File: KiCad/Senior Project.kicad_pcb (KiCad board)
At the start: 4 copper layers, 59.2 x 89.2 mm, 69 parts, among them J1 USB_C_Receptacle_USB2.0_16P, J2 Screw_Terminal_01x02, J3 Screw_Terminal_01x06, Q2 IRLML0030, Q3 IRLML0030, Q4 IRLML0030, SW1 SW_Push, SW2 SW_Push, U1 ESP32-S3FH4R2, U2 TPS62162DSG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

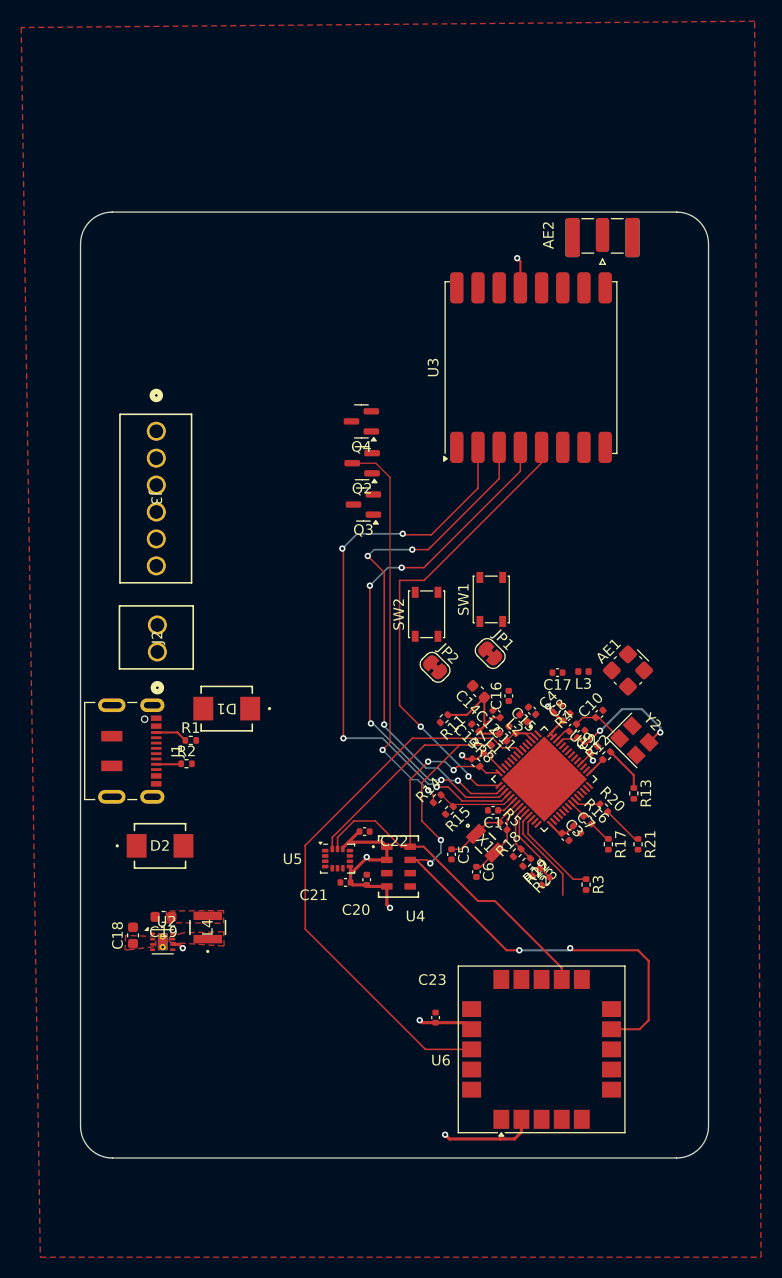
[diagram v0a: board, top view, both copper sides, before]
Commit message: Added power routing moved usb, and routed a couple signals to radio
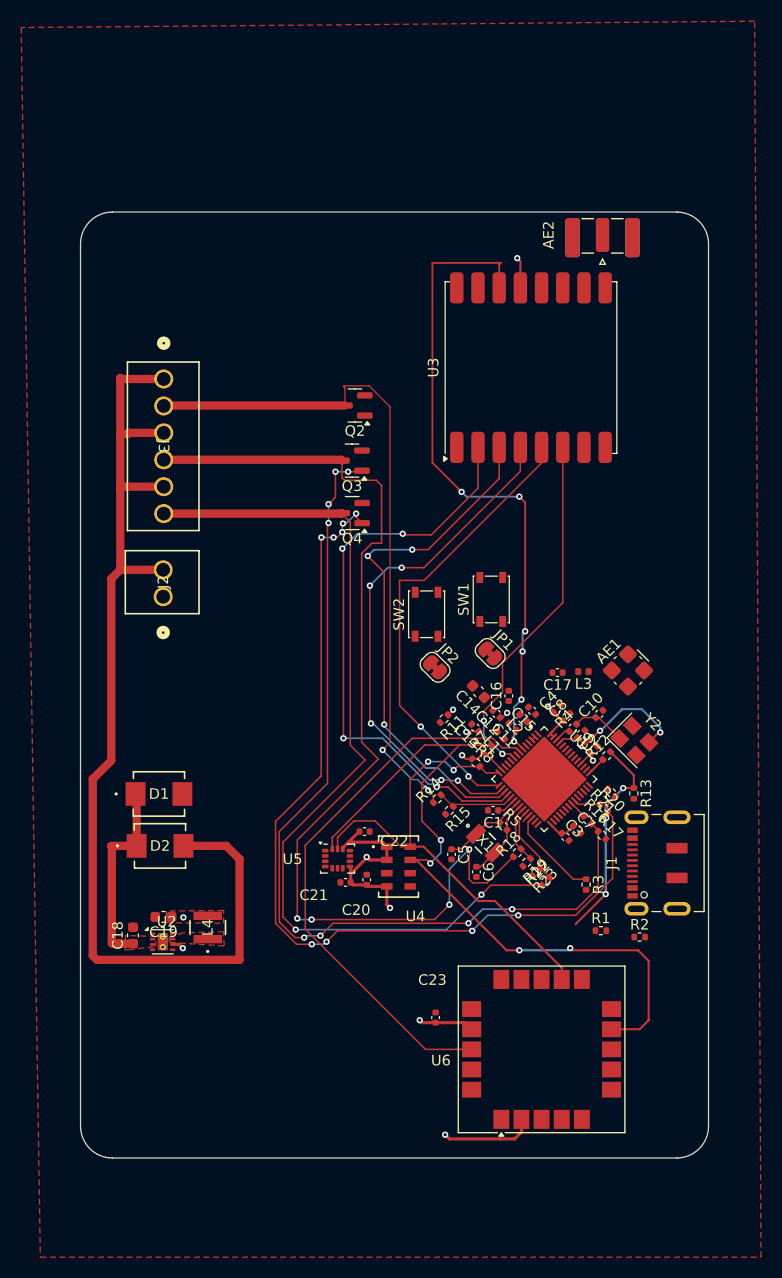
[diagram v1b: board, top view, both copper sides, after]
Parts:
- moved J1 52.1 mm to (179.1, 111.2), turned to 90 degrees
- moved R2 45.8 mm to (176.8, 118.2)
- moved R1 42.7 mm to (173.1, 117.5)
- moved D1 10.3 mm to (131.4, 104.7), turned to 0 degrees
- moved Q4 8.69 mm to (149.6, 78.2)
- moved Q2 5.49 mm to (149.9, 68.0)
- moved R21 5.46 mm to (174.1, 104.5), turned to 135 degrees
- moved J2 5.24 mm to (131.8, 86.0)
- moved J3 4.98 mm to (131.8, 65.5)
- moved Q3 4.28 mm to (149.6, 73.2)
- moved R17 1.04 mm to (173.2, 108.5), turned to -45 degrees
- moved C11 0.29 mm to (164.8, 98.3)
- moved L1 0.26 mm to (163.6, 99.1)
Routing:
- net +BATT: track 0.00 -> 101.4 mm
- net /Pyro Channel2/Pyro Pin: track 0.00 -> 97.6 mm, vias 0 -> 4
- net /Pyro Channel3/Pyro Pin: track 0.00 -> 85.7 mm, vias 0 -> 2
- net Net-(Q3-G): track 2.18 -> 86.1 mm, vias 0 -> 8
- net Net-(Q4-G): track 3.94 -> 87.5 mm, vias 0 -> 9
- net /Interrupt: track 0.00 -> 62.1 mm, vias 0 -> 6
- net /RADIO_RST: track 0.00 -> 34.0 mm, vias 0 -> 2
- net /Pyro Channel1/Pyro Pin: track 37.4 -> 64.1 mm
- net +VDC: track 0.00 -> 18.6 mm
- net Net-(Q2-G): track 4.32 -> 20.0 mm, vias 0 -> 2
- net +3V3: track 59.4 -> 50.2 mm, vias 9 -> 13
- net /USB_D-: track 9.32 -> 0.79 mm
- net /ESP-32 Power Coupler/VDD3P3: track 4.87 -> 0.59 mm
- net Net-(J1-CC1): track 3.05 -> 0.00 mm
- net Net-(J1-CC2): track 2.36 -> 0.00 mm
- added copper zone on In2.Cu, net +3V3
- removed copper zone on In1.Cu, net +3V3

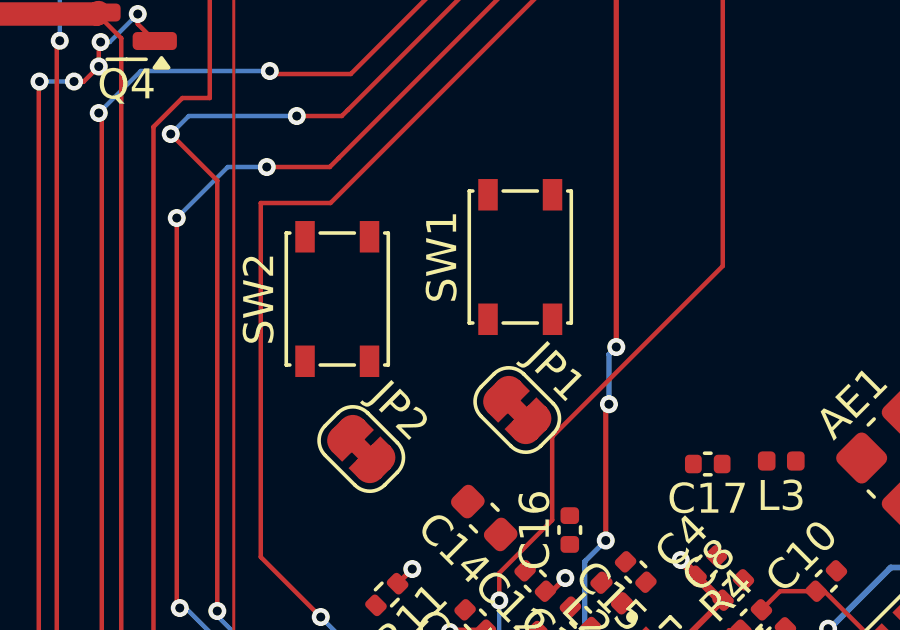
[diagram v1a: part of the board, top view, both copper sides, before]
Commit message: Added power routing moved usb, and more routing
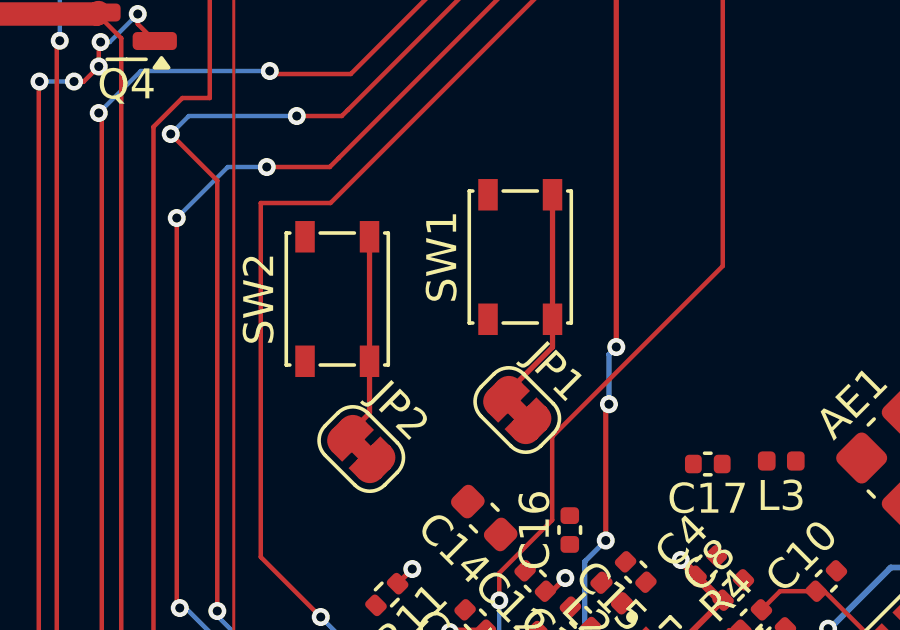
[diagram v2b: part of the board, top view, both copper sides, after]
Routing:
- net Net-(JP1-A): track 0.00 -> 7.39 mm
- net Net-(JP2-A): track 0.00 -> 6.92 mm
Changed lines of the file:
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@@
+	)
+	(segment
+		(start 163.825 88.375)
+		(end 163.825 84.225)
+		(width 0.175)
+		(layer "F.Cu")
+		(net 20)
+	)
+	(segment
+		(start 162.190381 90.940381)
+		(end 163.825 89.305762)
+		(width 0.175)
+		(layer "F.Cu")
+		(net 20)
+	)
+	(segment
+		(start 163.825 89.305762)
+		(end 163.825 88.375)
+		(width 0.175)
+		(layer "F.Cu")
+		(net 20)
+	)
+	(segment
+		(start 157.725 89.775)
+		(end 157.725 85.625)
+		(width 0.175)
+		(layer "F.Cu")
+		(net 23)
+	)
+	(segment
+		(start 157.725 91.505762)
+		(end 157.725 89.775)
+		(width 0.175)
+		(layer "F.Cu")
+		(net 23)
+	)
+	(segment
+		(start 156.990381 92.240381)
+		(end 157.725 91.505762)
+		(width 0.175)
+		(layer "F.Cu")
+		(net 23)
 	)
 	(segment

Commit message: Routing and placement
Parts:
- removed AE1: Antenna_Shield, RF_Antenna:Molex_47948-0001_2.4Ghz
- removed C10: 15p, Capacitor_SMD:C_0402_1005Metric
- removed C11, C12, C15, C16, C17, C9: 0.1uF, Capacitor_SMD:C_0402_1005Metric
- removed C13, C7, C8: 1uF, Capacitor_SMD:C_0402_1005Metric
- removed C14: 10uF, Capacitor_SMD:C_0603_1608Metric
- removed C5: 20pf, Capacitor_SMD:C_0402_1005Metric
- removed C6: 20p, Capacitor_SMD:C_0402_1005Metric
- removed JP1, JP2: SolderJumper_2_Bridged, Jumper:SolderJumper-2_P1.3mm_Bridged_RoundedPad1.0x1.5mm
- removed L1, L2, L3: 2.0nH, Inductor_SMD:L_0402_1005Metric
- removed R11: 100k, Resistor_SMD:R_0402_1005Metric
- removed R5: TBD, Capacitor_SMD:C_0402_1005Metric
- removed R7, R8: 10k, Resistor_SMD:R_0402_1005Metric
- removed SW2: SW_Push, Button_Switch_SMD:SW_SPST_PTS810
- removed X1: FC-135 32.7680KA-A5, FC-135:XTAL_FC-135_EPS
- removed Y2: Crystal_GND23, Crystal:Crystal_SMD_3225-4Pin_3.2x2.5mm
- added J5: Conn_01x03, Connector_PinHeader_2.54mm:PinHeader_1x03_P2.54mm_Vertical, F.Cu at (139.2, 87.3)
- C1: value 0.1uF -> 22 uF
- C2: value 15p -> 0.1 uF
- C3: value 0.1uF -> 0.1 uF
- C4: value 10nF -> 1 uF
- R4: value 24 nF -> 10k; footprint Capacitor_SMD:C_0402_1005Metric -> Resistor_SMD:R_0402_1005Metric
- U1: value ESP32-S3FH4R2 -> ESP32-S3-WROOM-1; footprint S3FH4R2:QFN40P700X700X90-57N -> RF_Module:ESP32-S3-WROOM-1U
- moved R20 38.7 mm to (151.1, 74.3)
- moved R12 38.7 mm to (151.3, 69.4)
- moved R13 38.7 mm to (153.9, 72.9)
- moved R16 38.7 mm to (149.6, 75.4)
- moved R17 38.7 mm to (150.9, 76.9)
- moved R21 38.7 mm to (151.8, 72.9)
- moved R19 30.3 mm to (142.0, 92.7), turned to 135 degrees
- moved R18 28.9 mm to (142.9, 91.8), turned to -45 degrees
- moved SW1 27.5 mm to (150.8, 111.1), turned to 180 degrees
- moved R2 23.0 mm to (173.6, 95.4), turned to 90 degrees
- moved R15 21.9 mm to (140.9, 93.6), turned to 135 degrees
- moved R14 20.8 mm to (139.8, 94.5), turned to -45 degrees
- moved C2 17.8 mm to (157.2, 109.9)
- moved R1 17.5 mm to (173.8, 100.1), turned to -90 degrees
- moved C4 16.2 mm to (160.9, 110.7)
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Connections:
- C2 pad 1: GND -> +3V3
- C2 pad 2: Net-(U1-XTAL_N) -> GND
- C3 pad 1: Net-(U1-VDD_SPI) -> GND
- C3 pad 2: GND -> /EN
- C4 pad 1: +3V3 -> GND
- C4 pad 2: GND -> /EN
- R4 pad 1: Net-(U1-XTAL_P) -> +3V3
- R4 pad 2: Net-(C10-Pad1) -> /EN
- SW1 pad 2: Net-(JP1-A) -> /EN
- U1 pad 1: /LNA Shield/LNA_IN -> GND
- U1 pad 10: unconnected-(U1-GPIO5-Pad10) -> /Pyro GPIO 1
- U1 pad 11: unconnected-(U1-GPIO6-Pad11) -> /Pyro GPIO 2
- U1 pad 13: /SDA -> /USB_D-
- U1 pad 14: /SCL -> /USB_D+
- U1 pad 15: /FSPICS0 -> unconnected-(U1-GPIO3/TOUCH3/ADC1_CH2-Pad15)
- U1 pad 16: /FSPID -> unconnected-(U1-GPIO46-Pad16)
- U1 pad 17: /FSPICLK -> /Interrupt
- U1 pad 18: /FSPIQ -> /FSPICS0
- U1 pad 19: /Sense 1 -> /FSPID
- U1 pad 2: /ESP-32 Power Coupler/VDD3P3 -> +3V3
- U1 pad 20: +3V3 -> /FSPICLK
- U1 pad 21: Net-(U1-XTAL_32K_P) -> /FSPIQ
- U1 pad 22: Net-(U1-XTAL_32K_N) -> /RADIO_RST
- U1 pad 23: /Sense 2 -> /Pyro GPIO 3
- U1 pad 24: /Sense 3 -> unconnected-(U1-GPIO47/SPICLK_P/SUBSPICLK_P_DIFF-Pad24)
- U1 pad 25: /USB_D- -> unconnected-(U1-GPIO48/SPICLK_N/SUBSPICLK_N_DIFF-Pad25)
- U1 pad 26: /USB_D+ -> unconnected-(U1-GPIO45-Pad26)
- U1 pad 29: Net-(U1-VDD_SPI) -> unconnected-(U1-SPIIO7/GPIO36/FSPICLK/SUBSPICLK-Pad29)
- U1 pad 3: /ESP-32 Power Coupler/VDD3P3 -> /EN
- U1 pad 32: unconnected-(U1-GPIO29/SPICS0-Pad32) -> /MTCK
- U1 pad 33: unconnected-(U1-GPIO30/SPICLK-Pad33) -> /MTD0
- U1 pad 34: unconnected-(U1-GPIO31/SPIQ-Pad34) -> /MTDI
- U1 pad 35: unconnected-(U1-GPIO32/SPID-Pad35) -> /MTMS
- U1 pad 36: /Pyro GPIO 2 -> /UORXD
- U1 pad 37: /Pyro GPIO 3 -> /UOTXD
- U1 pad 38: unconnected-(U1-GPIO33-Pad38) -> /Sense 2
- U1 pad 39: unconnected-(U1-GPIO34-Pad39) -> /Sense 1
- U1 pad 4: Net-(JP1-B) -> /GPS_Reset
- U1 pad 40: unconnected-(U1-GPIO35-Pad40) -> GND
- U1 pad 41: unconnected-(U1-GPIO36-Pad41) -> GND
- U1 pad 5: Net-(JP2-B) -> /SCL
- U1 pad 6: /Interrupt -> /SDA
- U1 pad 7: /GPS_Reset -> /Sense 3
- U1 pad 9: /RADIO_RST -> unconnected-(U1-GPIO16/U0CTS/ADC2_CH5/XTAL_32K_N-Pad9)
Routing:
- net +BATT: track 101.4 -> 0.00 mm
- net /Pyro Channel2/Pyro Pin: track 97.6 -> 0.00 mm, vias 4 -> 0
- net Net-(Q4-G): track 87.5 -> 0.00 mm, vias 9 -> 0
- net Net-(Q3-G): track 86.1 -> 0.00 mm, vias 8 -> 0
- net /Pyro Channel3/Pyro Pin: track 85.7 -> 0.00 mm, vias 2 -> 0
- net /Pyro Channel1/Pyro Pin: track 64.1 -> 0.00 mm, vias 2 -> 0
- net /Interrupt: track 62.1 -> 0.00 mm, vias 6 -> 0
- net /FSPIQ: track 55.3 -> 0.00 mm, vias 4 -> 0
- net /FSPICLK: track 49.7 -> 0.00 mm, vias 4 -> 0
- net /FSPID: track 49.0 -> 0.00 mm, vias 4 -> 0
- net /FSPICS0: track 43.9 -> 0.00 mm, vias 2 -> 0
- net GND: track 1.26 -> 37.2 mm
- net /RADIO_RST: track 34.0 -> 0.00 mm, vias 2 -> 0
- net /SDA: track 74.4 -> 45.1 mm, vias 4 -> 0
- net /GPS_Reset: track 53.3 -> 28.9 mm
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
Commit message: Routing
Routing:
- net /SDA: track 45.1 -> 85.0 mm, vias 0 -> 2
- net /SCL: track 35.7 -> 61.4 mm, vias 0 -> 2
- net /RADIO_RST: track 0.00 -> 22.0 mm, vias 0 -> 4
- net /FSPICS0: track 0.00 -> 20.7 mm
- net /FSPICLK: track 0.00 -> 19.0 mm, vias 0 -> 2
- net /FSPID: track 0.00 -> 18.5 mm
- net /FSPIQ: track 0.00 -> 16.7 mm
- net /Pyro GPIO 3: track 0.00 -> 3.94 mm
- net /GPS_Reset: track 28.9 -> 29.7 mm, vias 0 -> 2

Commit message: More routing
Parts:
- moved R13 7.01 mm to (148.9, 68.0), turned to 0 degrees
- moved R21 5.78 mm to (148.8, 77.8), turned to 0 degrees
- moved R20 5.23 mm to (148.8, 79.0), turned to 180 degrees
- moved R17 4.39 mm to (148.8, 73.0), turned to 0 degrees
- moved R12 2.45 mm to (148.9, 69.1), turned to 180 degrees
- moved R16 1.51 mm to (148.8, 74.1), turned to 180 degrees
- moved J1 0.81 mm to (179.2, 97.6)
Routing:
- net /Pyro Channel1/Pyro Pin: track 0.00 -> 12.6 mm
- net /Pyro Channel2/Pyro Pin: track 0.00 -> 12.4 mm
- net /Pyro Channel3/Pyro Pin: track 0.00 -> 12.4 mm
- net /Sense 1: track 0.00 -> 4.24 mm
- net /SDA: track 85.0 -> 81.1 mm
- net /Sense 2: track 0.00 -> 3.28 mm

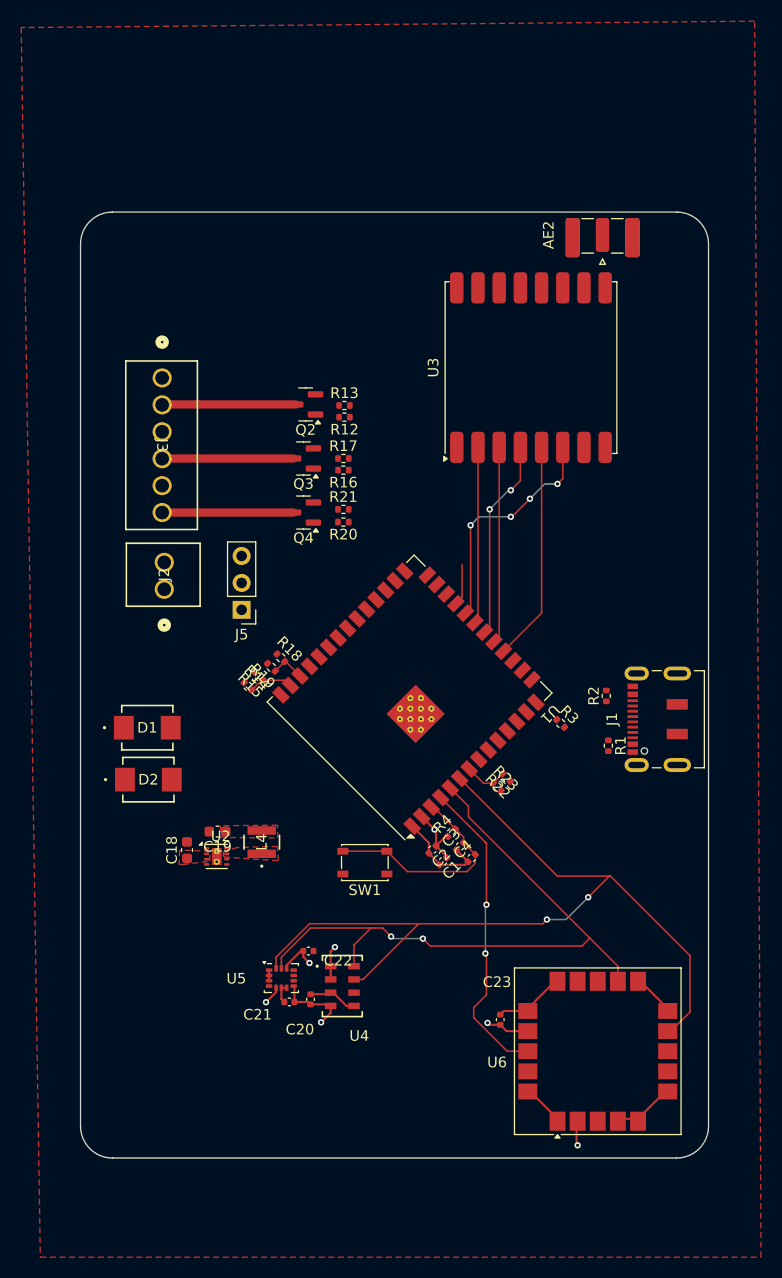
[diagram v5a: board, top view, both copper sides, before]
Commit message: DRC issues, only a few signals left to be routed
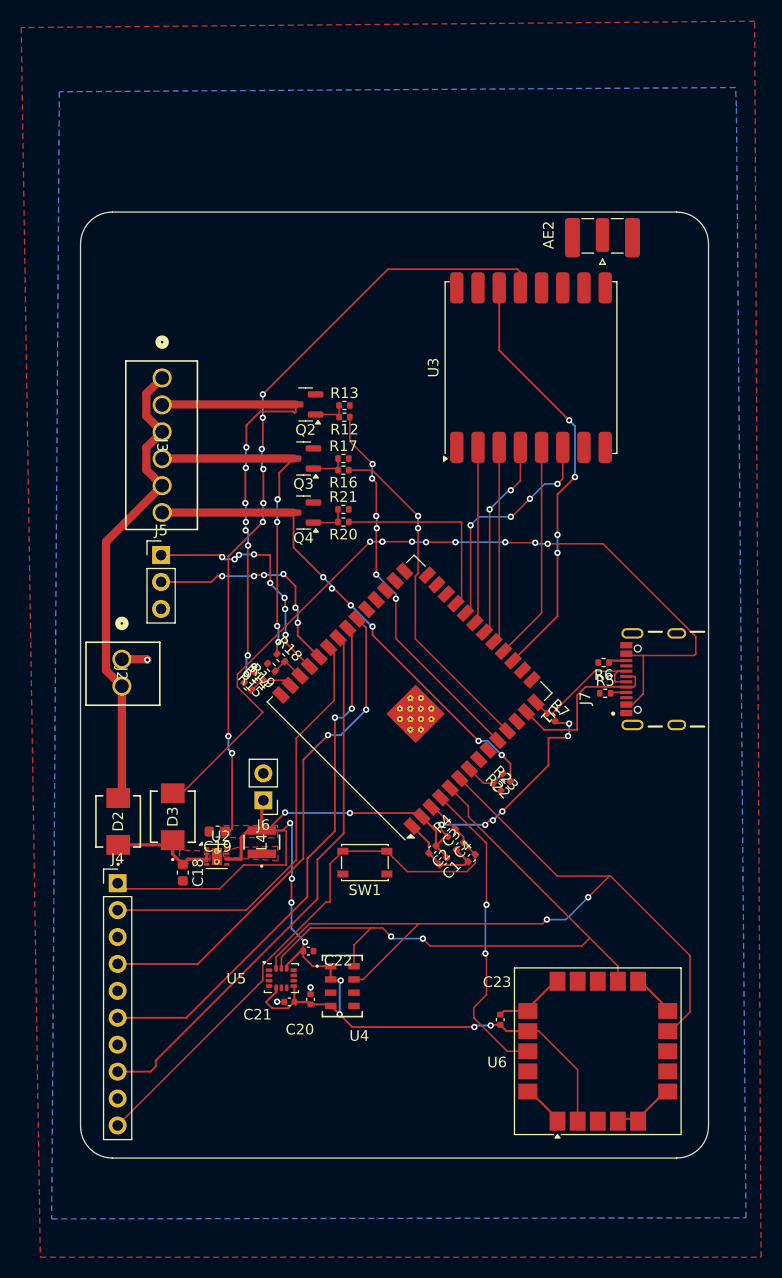
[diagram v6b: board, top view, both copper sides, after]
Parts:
- removed D1: D, VS_10BQ015HM3_5BT:CR_SMBDO-214AA_VIS
- removed J1: USB_C_Receptacle_USB2.0_16P, Connector_USB:USB_C_Receptacle_JAE_DX07S016JA1R1500
- removed R1, R2: 5.1k, Resistor_SMD:R_0402_1005Metric
- removed R3: 100k, Resistor_SMD:R_0402_1005Metric
- added D3: D, VS_10BQ015HM3_5BT:CR_SMBDO-214AA_VIS, F.Cu at (132.7, 106.8)
- added J4: Conn_ARM_JTAG_SWD_10, Connector_PinHeader_2.54mm:PinHeader_1x10_P2.54mm_Vertical, F.Cu at (127.5, 113.1)
- added J6: Conn_01x02, Connector_PinHeader_2.54mm:PinHeader_1x02_P2.54mm_Vertical, F.Cu at (141.2, 105.2)
- added J7: USB4105-GF-A, USB4105_GF_A (1):GCT_USB4105-GF-A, F.Cu at (180.2, 93.8)
- added R5: 5.1k, Resistor_SMD:R_0402_1005Metric, F.Cu at (173.5, 95.2)
- added R6: 5.1k, Resistor_SMD:R_0402_1005Metric, F.Cu at (173.3, 92.2)
- added R7: 100k, Resistor_SMD:R_0402_1005Metric, F.Cu at (168.4, 97.4)
- moved J5 9.19 mm to (131.6, 82.1), turned to 0 degrees
- moved J2 7.72 mm to (127.9, 91.9), turned to -90 degrees
- moved D2 4.87 mm to (127.5, 107.2), turned to 90 degrees
- moved C18 2.16 mm to (133.7, 112.1), turned to -90 degrees
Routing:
- net +3V3: track 28.6 -> 216.8 mm, vias 7 -> 24
- net Net-(D3-A): track 0.00 -> 82.6 mm, vias 0 -> 8
- net /MTDI: track 0.00 -> 51.8 mm
- net /MTD0: track 0.00 -> 50.4 mm, vias 0 -> 2
- net /MTCK: track 0.00 -> 47.8 mm, vias 0 -> 2
- net +BATT: track 0.00 -> 45.1 mm
- net /MTMS: track 0.00 -> 40.6 mm
- net /Interrupt: track 0.00 -> 40.6 mm, vias 0 -> 4
- net /Pyro GPIO 1: track 0.00 -> 36.4 mm, vias 0 -> 6
- net /EN: track 21.0 -> 55.9 mm
- net /Pyro Channel3/Pyro Pin: track 12.4 -> 46.9 mm, vias 0 -> 6
- net /Pyro GPIO 2: track 0.00 -> 32.3 mm, vias 0 -> 2
- net /Pyro Channel1/Pyro Pin: track 12.6 -> 43.2 mm, vias 0 -> 8
- net /UOTXD: track 0.00 -> 22.7 mm, vias 0 -> 8
- net /UORXD: track 0.00 -> 21.1 mm, vias 0 -> 6
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- added copper zone on B.Cu, net GND
- removed copper zone on In2.Cu, net +3V3
